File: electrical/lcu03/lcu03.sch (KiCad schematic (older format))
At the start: 91 parts

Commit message: It looks like completed schematics.
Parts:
- removed P?: ext, Socket_Strips:Socket_Strip_Angled_1x13, symbol CONN_01X13
- added P?: ext, symbol CONN_01X12
- R? (x2): value 30k 5% -> 33k 5%
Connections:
- net labels removed: gpio-4
- wire segments 346 -> 345
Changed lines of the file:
@@
 Text Label 9700 6950 0    60   ~ 0
 gpio-3
-Text Label 9700 7150 0    60   ~ 0
-gpio-4
 Text Label 2700 12550 0    60   ~ 0
 tx-2
@@
 	1    0    0    -1
 $EndComp
-Text Label 2950 13750 0    60   ~ 0
+Text Label 2950 13650 0    60   ~ 0
 Vbus
 $Comp
-L CONN_01X13 P?
-U 1 1 56676C80
-P 2400 13150
-F 0 "P?" H 2400 13850 50  0000 C CNN
-F 1 "ext" V 2500 13150 50  0000 C CNN
-F 2 "Socket_Strips:Socket_Strip_Angled_1x13" H 2400 13150 60  0001 C CNN
-F 3 "" H 2400 13150 60  0000 C CNN
-	1    2400 13150
-	-1   0    0    -1
-$EndComp
-$Comp
 L GND #PWR?
 U 1 1 56676C81
-P 3550 13750
-F 0 "#PWR?" H 3550 13500 50  0001 C CNN
-F 1 "GND" H 3550 13600 50  0000 C CNN
-F 2 "" H 3550 13750 60  0000 C CNN
-F 3 "" H 3550 13750 60  0000 C CNN
-	1    3550 13750
+P 3550 13650
+F 0 "#PWR?" H 3550 13400 50  0001 C CNN
+F 1 "GND" H 3550 13500 50  0000 C CNN
+F 2 "" H 3550 13650 60  0000 C CNN
+F 3 "" H 3550 13650 60  0000 C CNN
+	1    3550 13650
 	1    0    0    -1
 $EndComp
@@
 Text Label 2700 13450 0    60   ~ 0
 gpio-3
-Text Label 2700 13550 0    60   ~ 0
-gpio-4
 $Comp
 L PWR_FLAG #FLG?
@@
 	9150 6950 10000 6950
 Wire Wire Line
-	9150 7150 10000 7150
-Wire Wire Line
 	9150 7500 10000 7500
 Wire Wire Line
@@
 	2600 13450 3000 13450
 Wire Wire Line
-	2600 13550 3000 13550
-Wire Wire Line
-	2600 13750 3150 13750
-Wire Wire Line
-	2600 13650 3550 13650
-Wire Wire Line
-	3550 13650 3550 13750
+	2600 13650 3150 13650
+Wire Wire Line
+	2600 13550 3550 13550
+Wire Wire Line
+	3550 13550 3550 13650
 Wire Wire Line
 	2600 12850 3000 12850
@@
 P 27450 5200
 F 0 "R?" V 27530 5200 50  0000 C CNN
-F 1 "1k 5%" V 27450 5200 50  0000 C CNN
+F 1 "1k 5%" V 27550 5450 50  0000 C CNN
 F 2 "" V 27380 5200 50  0000 C CNN
 F 3 "" H 27450 5200 50  0000 C CNN
@@
 P 27200 5450
 F 0 "R?" V 27280 5450 50  0000 C CNN
-F 1 "30k 5%" V 27200 5450 50  0000 C CNN
+F 1 "33k 5%" V 27100 5450 50  0000 C CNN
 F 2 "" V 27130 5450 50  0000 C CNN
 F 3 "" H 27200 5450 50  0000 C CNN
@@
 P 29750 5200
 F 0 "R?" V 29830 5200 50  0000 C CNN
-F 1 "1k 5%" V 29750 5200 50  0000 C CNN
+F 1 "1k 5%" V 29850 5450 50  0000 C CNN
 F 2 "" V 29680 5200 50  0000 C CNN
 F 3 "" H 29750 5200 50  0000 C CNN
@@
 P 29500 5450
 F 0 "R?" V 29580 5450 50  0000 C CNN
-F 1 "30k 5%" V 29500 5450 50  0000 C CNN
+F 1 "33k 5%" V 29400 5450 50  0000 C CNN
 F 2 "" V 29430 5450 50  0000 C CNN
 F 3 "" H 29500 5450 50  0000 C CNN
@@
 Wire Notes Line
 	6500 22350 6250 22100
+Text Label 9200 7150 0    60   ~ 0
+~wc~
+Wire Wire Line
+	9150 7150 9400 7150
+$Comp
+L CONN_01X12 P?
+U 1 1 566D8BB6
+P 2400 13100
+F 0 "P?" H 2400 13750 50  0000 C CNN
+F 1 "ext" V 2500 13100 50  0000 C CNN
+F 2 "" H 2400 13100 50  0000 C CNN
+F 3 "" H 2400 13100 50  0000 C CNN
+	1    2400 13100
+	-1   0    0    -1
+$EndComp
 $EndSCHEMATC

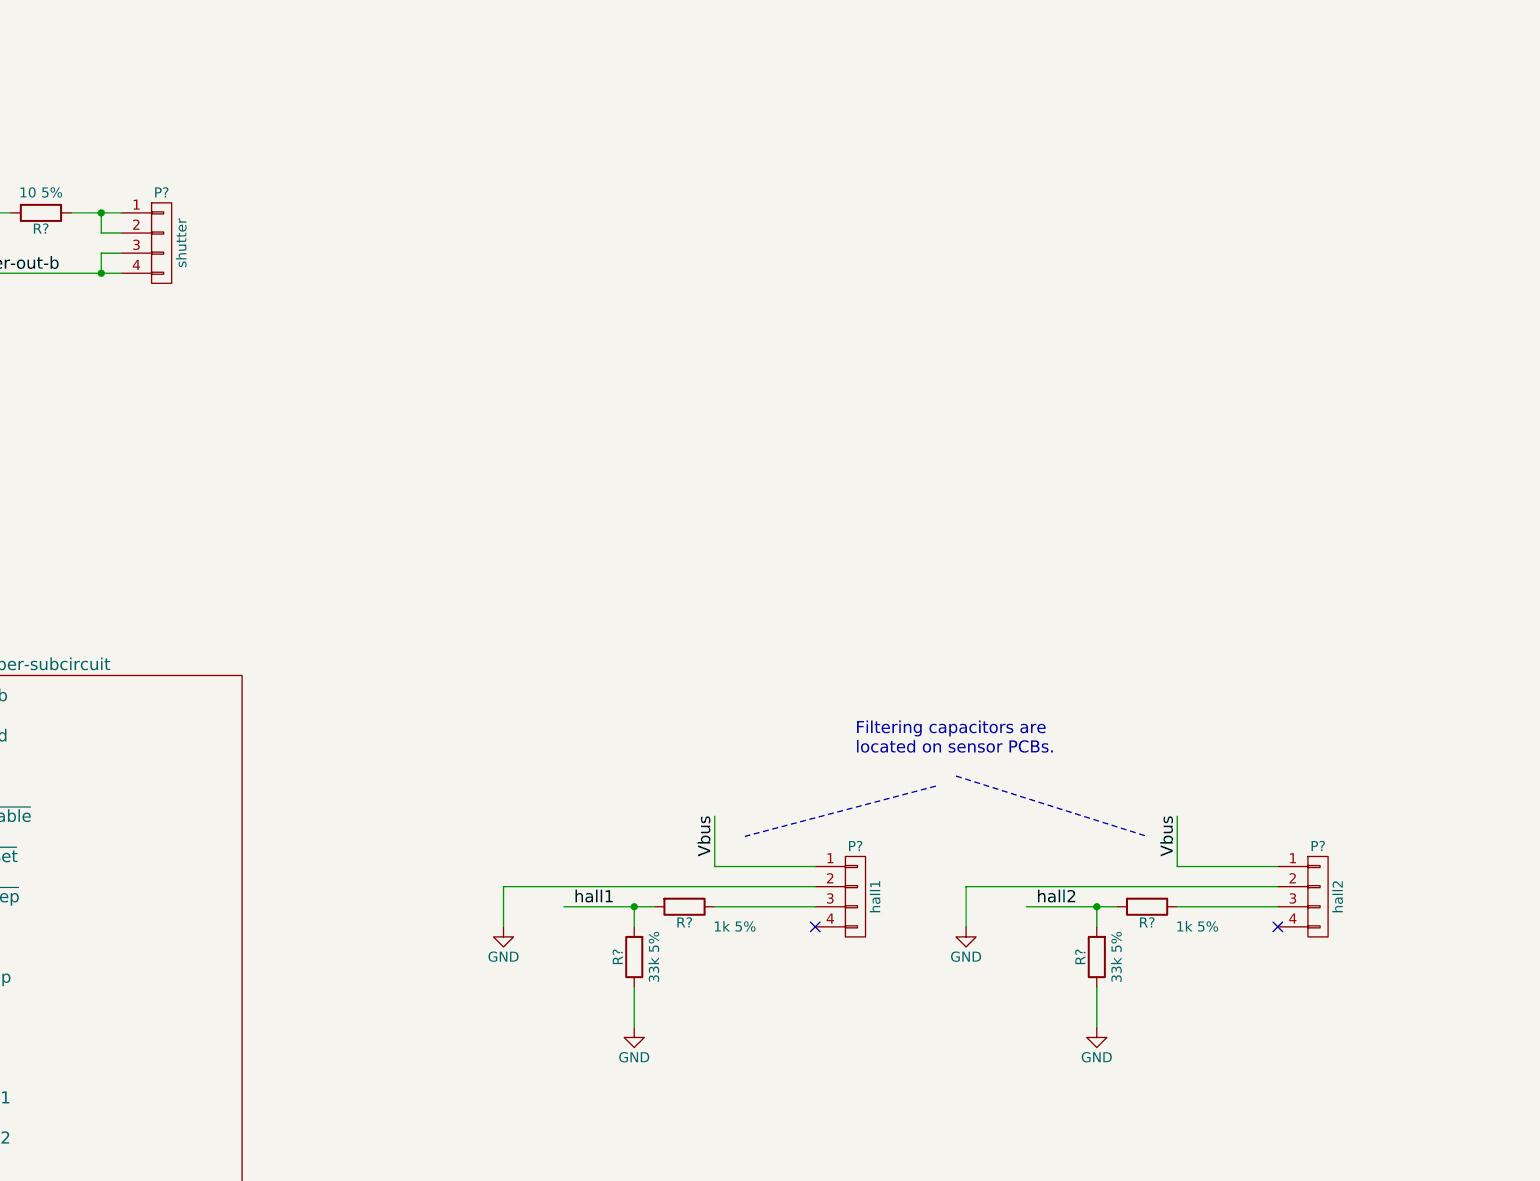
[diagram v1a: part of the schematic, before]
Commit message: Added specific socket used for stepper motors and for sensors.
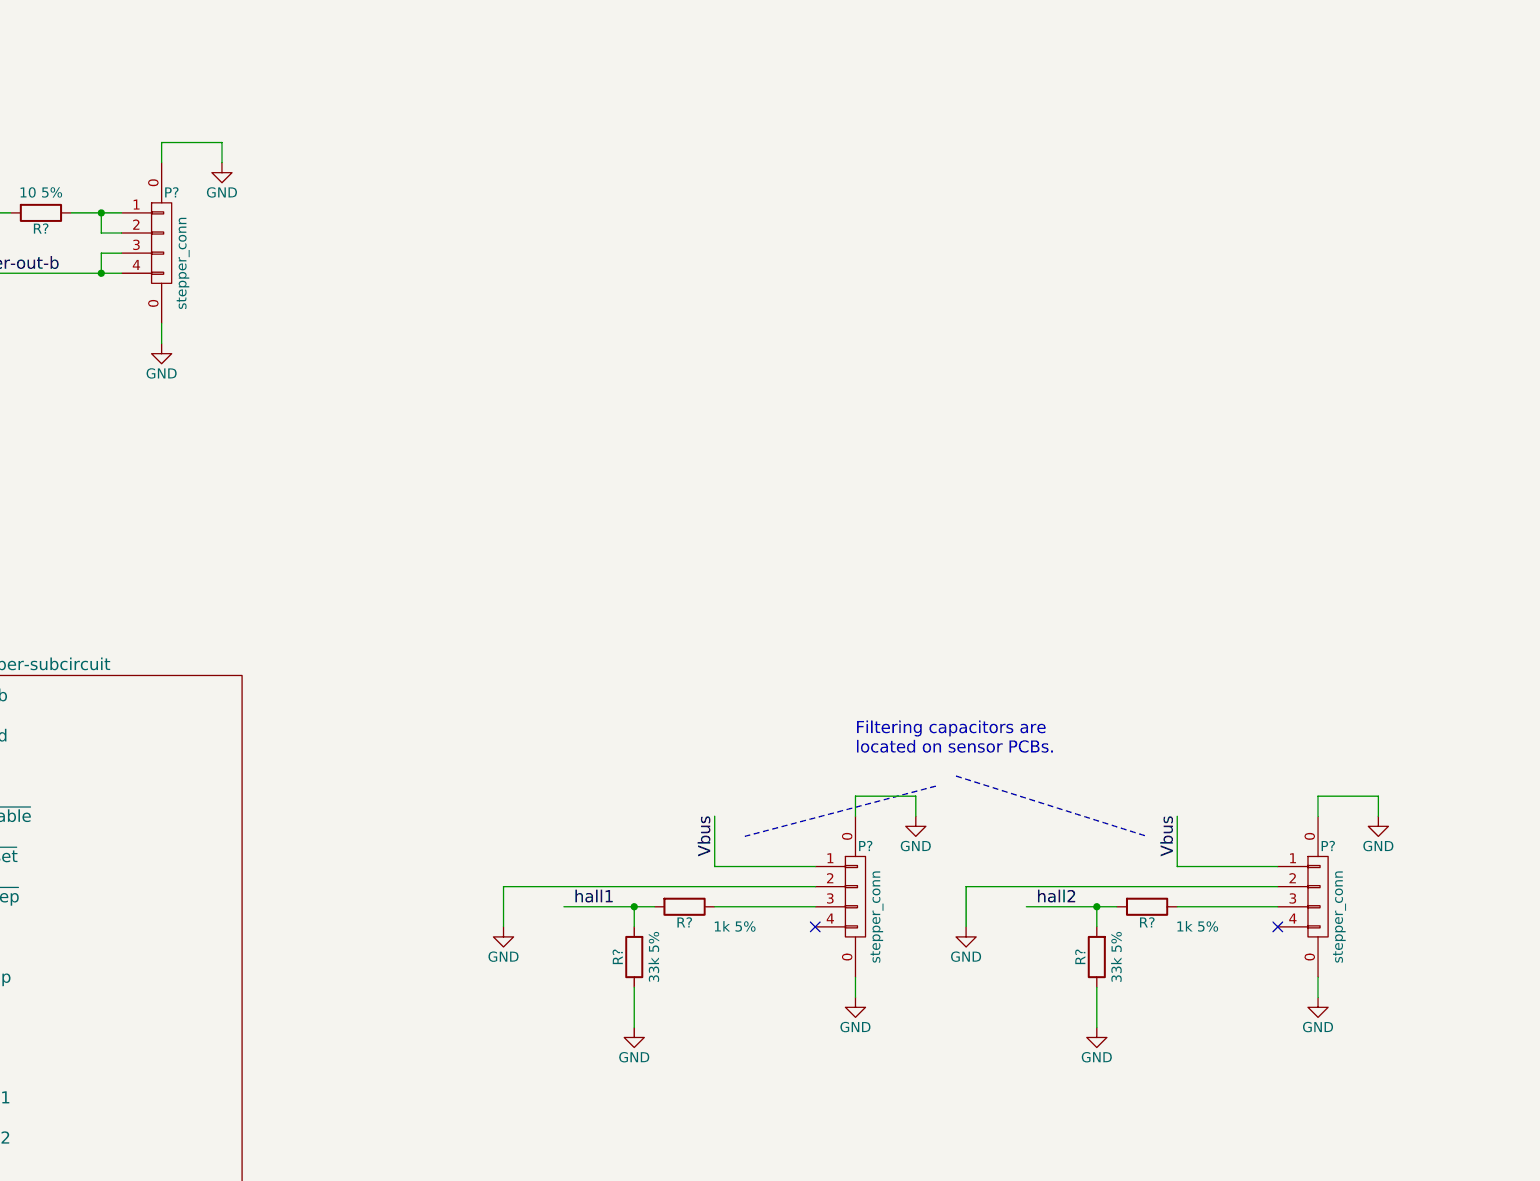
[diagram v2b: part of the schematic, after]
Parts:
- removed P?: hall1, symbol CONN_01X04
- removed P?: hall2, symbol CONN_01X04
- removed P?: shutter, symbol CONN_01X04
- added P? (x3): stepper_conn, symbol stepper_conn
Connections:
- wire segments 345 -> 357
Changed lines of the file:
@@
 LIBS:ts881
 LIBS:m24c02
+LIBS:stepper_conn
 LIBS:lcu03-cache
 EELAYER 25 0
@@
 Text Label 23200 5750 0    60   ~ 0
 dir2
-$Comp
-L CONN_01X04 P?
-U 1 1 5668A725
-P 28300 5150
-F 0 "P?" H 28300 5400 50  0000 C CNN
-F 1 "hall1" V 28400 5150 50  0000 C CNN
-F 2 "" H 28300 5150 50  0000 C CNN
-F 3 "" H 28300 5150 50  0000 C CNN
-	1    28300 5150
-	1    0    0    -1
-$EndComp
 Wire Wire Line
 	28100 5000 27600 5000
@@
 Text Label 26900 5200 0    60   ~ 0
 hall1
-$Comp
-L CONN_01X04 P?
-U 1 1 566909B9
-P 30600 5150
-F 0 "P?" H 30600 5400 50  0000 C CNN
-F 1 "hall2" V 30700 5150 50  0000 C CNN
-F 2 "" H 30600 5150 50  0000 C CNN
-F 3 "" H 30600 5150 50  0000 C CNN
-	1    30600 5150
-	1    0    0    -1
-$EndComp
 Wire Wire Line
 	30400 5000 29900 5000
@@
 Text Label 29200 5200 0    60   ~ 0
 hall2
-$Comp
-L CONN_01X04 P?
-U 1 1 56693F22
-P 24850 1900
-F 0 "P?" H 24850 2150 50  0000 C CNN
-F 1 "shutter" V 24950 1900 50  0000 C CNN
-F 2 "" H 24850 1900 50  0000 C CNN
-F 3 "" H 24850 1900 50  0000 C CNN
-	1    24850 1900
-	1    0    0    -1
-$EndComp
 $Comp
 L R R?
@@
 	-1   0    0    -1
 $EndComp
+$Comp
+L stepper_conn P?
+U 1 1 5668ADE1
+P 24850 1900
+F 0 "P?" H 24900 2150 50  0000 C CNN
+F 1 "stepper_conn" V 24950 1800 50  0000 C CNN
+F 2 "" H 24850 1900 50  0000 C CNN
+F 3 "" H 24850 1900 50  0000 C CNN
+	1    24850 1900
+	1    0    0    -1
+$EndComp
+Wire Wire Line
+	24850 1500 24850 1400
+Wire Wire Line
+	24850 1400 25150 1400
+Wire Wire Line
+	25150 1400 25150 1500
+Wire Wire Line
+	24850 2300 24850 2400
+$Comp
+L GND #PWR?
+U 1 1 5668B645
+P 24850 2400
+F 0 "#PWR?" H 24850 2150 50  0001 C CNN
+F 1 "GND" H 24850 2250 50  0000 C CNN
+F 2 "" H 24850 2400 60  0000 C CNN
+F 3 "" H 24850 2400 60  0000 C CNN
+	1    24850 2400
+	1    0    0    -1
+$EndComp
+$Comp
+L GND #PWR?
+U 1 1 5668B7D9
+P 25150 1500
+F 0 "#PWR?" H 25150 1250 50  0001 C CNN
+F 1 "GND" H 25150 1350 50  0000 C CNN
+F 2 "" H 25150 1500 60  0000 C CNN
+F 3 "" H 25150 1500 60  0000 C CNN
+	1    25150 1500
+	1    0    0    -1
+$EndComp
+$Comp
+L stepper_conn P?
+U 1 1 5668C43A
+P 28300 5150
+F 0 "P?" H 28350 5400 50  0000 C CNN
+F 1 "stepper_conn" V 28400 5050 50  0000 C CNN
+F 2 "" H 28300 5150 50  0000 C CNN
+F 3 "" H 28300 5150 50  0000 C CNN
+	1    28300 5150
+	1    0    0    -1
+$EndComp
+Wire Wire Line
+	28300 4750 28300 4650
+Wire Wire Line
+	28300 4650 28600 4650
+Wire Wire Line
+	28600 4650 28600 4750
+Wire Wire Line
+	28300 5550 28300 5650
+$Comp
+L GND #PWR?
+U 1 1 5668C444
+P 28300 5650
+F 0 "#PWR?" H 28300 5400 50  0001 C CNN
+F 1 "GND" H 28300 5500 50  0000 C CNN
+F 2 "" H 28300 5650 60  0000 C CNN
+F 3 "" H 28300 5650 60  0000 C CNN
+	1    28300 5650
+	1    0    0    -1
+$EndComp
+$Comp
+L GND #PWR?
+U 1 1 5668C44A
+P 28600 4750
+F 0 "#PWR?" H 28600 4500 50  0001 C CNN
+F 1 "GND" H 28600 4600 50  0000 C CNN
+F 2 "" H 28600 4750 60  0000 C CNN
+F 3 "" H 28600 4750 60  0000 C CNN
+	1    28600 4750
+	1    0    0    -1
+$EndComp
+$Comp
+L stepper_conn P?
+U 1 1 5668E474
+P 30600 5150
+F 0 "P?" H 30650 5400 50  0000 C CNN
+F 1 "stepper_conn" V 30700 5050 50  0000 C CNN
+F 2 "" H 30600 5150 50  0000 C CNN
+F 3 "" H 30600 5150 50  0000 C CNN
+	1    30600 5150
+	1    0    0    -1
+$EndComp
+Wire Wire Line
+	30600 4750 30600 4650
+Wire Wire Line
+	30600 4650 30900 4650
+Wire Wire Line
+	30900 4650 30900 4750
+Wire Wire Line
+	30600 5550 30600 5650
+$Comp
+L GND #PWR?
+U 1 1 5668E47E
+P 30600 5650
+F 0 "#PWR?" H 30600 5400 50  0001 C CNN
+F 1 "GND" H 30600 5500 50  0000 C CNN
+F 2 "" H 30600 5650 60  0000 C CNN
+F 3 "" H 30600 5650 60  0000 C CNN
+	1    30600 5650
+	1    0    0    -1
+$EndComp
+$Comp
+L GND #PWR?
+U 1 1 5668E484
+P 30900 4750
+F 0 "#PWR?" H 30900 4500 50  0001 C CNN
+F 1 "GND" H 30900 4600 50  0000 C CNN
+F 2 "" H 30900 4750 60  0000 C CNN
+F 3 "" H 30900 4750 60  0000 C CNN
+	1    30900 4750
+	1    0    0    -1
+$EndComp
 $EndSCHEMATC

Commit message: a
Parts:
- removed P?: ext, symbol CONN_01X12
- added C?: 100n, symbol C
- added P?: ext-2, symbol CONN_01X08
- added P?: ext-1, symbol CONN_01X08
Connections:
- wire segments 357 -> 367
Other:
- moved on the sheet: C?, L?
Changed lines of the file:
@@
 	1    0    0    -1
 $EndComp
-Text Label 2950 13650 0    60   ~ 0
+Text Label 2950 13150 0    60   ~ 0
 Vbus
-$Comp
-L GND #PWR?
-U 1 1 56676C81
-P 3550 13650
-F 0 "#PWR?" H 3550 13400 50  0001 C CNN
-F 1 "GND" H 3550 13500 50  0000 C CNN
-F 2 "" H 3550 13650 60  0000 C CNN
-F 3 "" H 3550 13650 60  0000 C CNN
-	1    3550 13650
-	1    0    0    -1
-$EndComp
-Text Label 2700 13150 0    60   ~ 0
-gpio-0
-Text Label 2700 13250 0    60   ~ 0
-gpio-1
-Text Label 2700 13350 0    60   ~ 0
-gpio-2
-Text Label 2700 13450 0    60   ~ 0
-gpio-3
 $Comp
 L PWR_FLAG #FLG?
@@
 	3550 13050 3550 13150
 Wire Wire Line
-	2600 13150 3000 13150
-Wire Wire Line
-	2600 13250 3000 13250
-Wire Wire Line
-	2600 13350 3000 13350
-Wire Wire Line
-	2600 13450 3000 13450
-Wire Wire Line
-	2600 13650 3150 13650
-Wire Wire Line
-	2600 13550 3550 13550
-Wire Wire Line
-	3550 13550 3550 13650
+	2600 13150 3150 13150
 Wire Wire Line
 	2600 12850 3000 12850
@@
 L CP C?
 U 1 1 5667DB4D
-P 18550 2800
-F 0 "C?" H 18575 2900 50  0000 L CNN
-F 1 "680u" H 18575 2700 50  0000 L CNN
-F 2 "Capacitors_ThroughHole:C_Radial_D10_L20_P5" H 18588 2650 30  0001 C CNN
-F 3 "" H 18550 2800 60  0000 C CNN
-	1    18550 2800
-	1    0    0    -1
-$EndComp
-Wire Wire Line
-	18550 2950 18550 3200
+P 17350 5450
+F 0 "C?" H 17375 5550 50  0000 L CNN
+F 1 "680u" H 17375 5350 50  0000 L CNN
+F 2 "Capacitors_ThroughHole:C_Radial_D10_L20_P5" H 17388 5300 30  0001 C CNN
+F 3 "" H 17350 5450 60  0000 C CNN
+	1    17350 5450
+	1    0    0    -1
+$EndComp
+Wire Wire Line
+	17350 5600 17350 5850
 $Comp
 L GND #PWR?
 U 1 1 5667E5F0
-P 18550 3200
-F 0 "#PWR?" H 18550 2950 50  0001 C CNN
-F 1 "GND" H 18550 3050 50  0000 C CNN
-F 2 "" H 18550 3200 50  0000 C CNN
-F 3 "" H 18550 3200 50  0000 C CNN
-	1    18550 3200
-	1    0    0    -1
-$EndComp
-Text Label 18550 1850 1    60   ~ 0
+P 17350 5850
+F 0 "#PWR?" H 17350 5600 50  0001 C CNN
+F 1 "GND" H 17350 5700 50  0000 C CNN
+F 2 "" H 17350 5850 50  0000 C CNN
+F 3 "" H 17350 5850 50  0000 C CNN
+	1    17350 5850
+	1    0    0    -1
+$EndComp
+Text Label 17350 4500 1    60   ~ 0
 v+
 $Comp
@@
 L INDUCTOR L?
 U 1 1 566B3253
-P 18550 2250
-F 0 "L?" V 18500 2250 50  0000 C CNN
-F 1 "10uH" V 18650 2250 50  0000 C CNN
-F 2 "my-lib:my_inductance" H 18550 2250 60  0001 C CNN
-F 3 "" H 18550 2250 60  0000 C CNN
-	1    18550 2250
+P 17350 4900
+F 0 "L?" V 17300 4900 50  0000 C CNN
+F 1 "10uH" V 17450 4900 50  0000 C CNN
+F 2 "my-lib:my_inductance" H 17350 4900 60  0001 C CNN
+F 3 "" H 17350 4900 60  0000 C CNN
+	1    17350 4900
 	-1   0    0    1
 $EndComp
 Wire Wire Line
-	18550 1950 18550 1750
-Wire Wire Line
-	18550 2650 18550 2550
-Wire Wire Line
-	18550 2600 19150 2600
-Connection ~ 18550 2600
-Text Label 18750 2600 0    60   ~ 0
+	17350 4600 17350 4400
+Wire Wire Line
+	17350 5300 17350 5200
+Wire Wire Line
+	17350 5250 17950 5250
+Connection ~ 17350 5250
+Text Label 17550 5250 0    60   ~ 0
 Vmotors
 Text Label 20150 1250 1    60   ~ 0
@@
 	9150 7150 9400 7150
 $Comp
-L CONN_01X12 P?
-U 1 1 566D8BB6
-P 2400 13100
-F 0 "P?" H 2400 13750 50  0000 C CNN
-F 1 "ext" V 2500 13100 50  0000 C CNN
-F 2 "" H 2400 13100 50  0000 C CNN
-F 3 "" H 2400 13100 50  0000 C CNN
-	1    2400 13100
-	-1   0    0    -1
-$EndComp
-$Comp
 L stepper_conn P?
 U 1 1 5668ADE1
@@
 	1    0    0    -1
 $EndComp
+Wire Wire Line
+	17800 9100 17800 9350
+$Comp
+L GND #PWR?
+U 1 1 566E5DF8
+P 17800 9350
+F 0 "#PWR?" H 17800 9100 50  0001 C CNN
+F 1 "GND" H 17800 9200 50  0000 C CNN
+F 2 "" H 17800 9350 50  0000 C CNN
+F 3 "" H 17800 9350 50  0000 C CNN
+	1    17800 9350
+	1    0    0    -1
+$EndComp
+$Comp
+L C C?
+U 1 1 566E5DFE
+P 17800 8950
+F 0 "C?" H 17825 9050 50  0000 L CNN
+F 1 "100n" H 17825 8850 50  0000 L CNN
+F 2 "" H 17838 8800 50  0000 C CNN
+F 3 "" H 17800 8950 50  0000 C CNN
+	1    17800 8950
+	1    0    0    -1
+$EndComp
+Wire Wire Line
+	17800 8800 17800 8600
+$Comp
+L VDD #PWR?
+U 1 1 566E5E05
+P 17800 8600
+F 0 "#PWR?" H 17800 8450 50  0001 C CNN
+F 1 "VDD" H 17800 8750 50  0000 C CNN
+F 2 "" H 17800 8600 60  0000 C CNN
+F 3 "" H 17800 8600 60  0000 C CNN
+	1    17800 8600
+	1    0    0    -1
+$EndComp
+Wire Wire Line
+	4750 12550 4850 12550
+Wire Wire Line
+	4850 12550 4850 12450
+$Comp
+L VDD #PWR?
+U 1 1 566E993D
+P 4850 12450
+F 0 "#PWR?" H 4850 12550 30  0001 C CNN
+F 1 "VDD" H 4850 12560 30  0000 C CNN
+F 2 "" H 4850 12450 60  0000 C CNN
+F 3 "" H 4850 12450 60  0000 C CNN
+	1    4850 12450
+	1    0    0    -1
+$EndComp
+Wire Wire Line
+	4750 12650 5900 12650
+Wire Wire Line
+	5900 12650 5900 12750
+$Comp
+L GND #PWR?
+U 1 1 566E9D28
+P 5900 12750
+F 0 "#PWR?" H 5900 12500 50  0001 C CNN
+F 1 "GND" H 5900 12600 50  0000 C CNN
+F 2 "" H 5900 12750 60  0000 C CNN
+F 3 "" H 5900 12750 60  0000 C CNN
+	1    5900 12750
+	1    0    0    -1
+$EndComp
+Wire Wire Line
+	4750 12750 5000 12750
+Text Label 4900 12750 0    60   ~ 0
+v+
+Wire Wire Line
+	4750 12850 5600 12850
+Wire Wire Line
+	5600 12850 5600 12950
+$Comp
+L GND #PWR?
+U 1 1 566EBD7A
+P 5600 12950
+F 0 "#PWR?" H 5600 12700 50  0001 C CNN
+F 1 "GND" H 5600 12800 50  0000 C CNN
+F 2 "" H 5600 12950 60  0000 C CNN
+F 3 "" H 5600 12950 60  0000 C CNN
+	1    5600 12950
+	1    0    0    -1
+$EndComp
+$Comp
+L CONN_01X08 P?
+U 1 1 566EBEB9
+P 4550 12900
+F 0 "P?" H 4550 13350 50  0000 C CNN
+F 1 "ext-2" V 4650 12900 50  0000 C CNN
+F 2 "" H 4550 12900 50  0000 C CNN
+F 3 "" H 4550 12900 50  0000 C CNN
+	1    4550 12900
+	-1   0    0    -1
+$EndComp
+Text Label 4850 12950 0    60   ~ 0
+gpio-0
+Text Label 4850 13050 0    60   ~ 0
+gpio-1
+Text Label 4850 13150 0    60   ~ 0
+gpio-2
+Text Label 4850 13250 0    60   ~ 0
+gpio-3
+Wire Wire Line
+	4750 12950 5150 12950
+Wire Wire Line
+	4750 13050 5150 13050
+Wire Wire Line
+	4750 13150 5150 13150
+Wire Wire Line
+	4750 13250 5150 13250
+$Comp
+L CONN_01X08 P?
+U 1 1 566ED417
+P 2400 12900
+F 0 "P?" H 2400 13350 50  0000 C CNN
+F 1 "ext-1" V 2500 12900 50  0000 C CNN
+F 2 "" H 2400 12900 50  0000 C CNN
+F 3 "" H 2400 12900 50  0000 C CNN
+	1    2400 12900
+	-1   0    0    -1
+$EndComp
+Wire Wire Line
+	2600 13250 3350 13250
+Wire Wire Line
+	3350 13250 3350 13350
+$Comp
+L GND #PWR?
+U 1 1 566EF91F
+P 3350 13350
+F 0 "#PWR?" H 3350 13100 50  0001 C CNN
+F 1 "GND" H 3350 13200 50  0000 C CNN
+F 2 "" H 3350 13350 60  0000 C CNN
+F 3 "" H 3350 13350 60  0000 C CNN
+	1    3350 13350
+	1    0    0    -1
+$EndComp
+$Comp
+L PWR_FLAG #FLG?
+U 1 1 566F377F
+P 17950 5100
+F 0 "#FLG?" H 17950 5195 50  0001 C CNN
+F 1 "PWR_FLAG" H 17950 5280 50  0000 C CNN
+F 2 "" H 17950 5100 60  0000 C CNN
+F 3 "" H 17950 5100 60  0000 C CNN
+	1    17950 5100
+	1    0    0    -1
+$EndComp
+Wire Wire Line
+	17950 5250 17950 5100
 $EndSCHEMATC

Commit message: Added KiCad footprint libraries in file system as there are some troubles with access to them via github.com.
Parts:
- gave numbers to parts that had none: 93

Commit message: a
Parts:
- C14, C23: footprint (none) -> Capacitors_SMD:C_0805_HandSoldering
- C26: footprint (none) -> Capacitors_SMD:C_0805
- L1: footprint my-lib:my_inductance -> Resistors_SMD:R_1206_HandSoldering
- P1, P2, P3, P4: footprint Divers:douille_4mm -> Mounting_Holes:MountingHole_3mm
- P11, P12, P13: footprint (none) -> Connectors_JST_PH:Connectors_JST_B4B-PH-SM4-TB
- P5, P8: footprint (none) -> Pin_Headers:Pin_Header_Angled_1x08
- Q1, Q2, Q3: footprint (none) -> TO_SOT_Packages_SMD:SOT-23_Handsoldering
- R10, R11, R12, R13, R16, R24, R25: footprint Resistors_SMD:R_0805_HandSoldering -> Resistors_SMD:R_0805
- R14, R15, R17, R18, R19, R20, R21, R22, R23, R26, R27, R28, R29, R30, R31, R32, R33, R34, R35, R36, R9: footprint (none) -> Resistors_SMD:R_0805
- U3: footprint (none) -> Housings_SOIC:SOIC-8_3.9x4.9mm_Pitch1.27mm
- U5: footprint Housings_SOT-23_SOT-143_TSOT-6:SOT-23 -> TO_SOT_Packages_SMD:SOT-23_Handsoldering
- U6: footprint (none) -> TO_SOT_Packages_SMD:SOT-23-5
